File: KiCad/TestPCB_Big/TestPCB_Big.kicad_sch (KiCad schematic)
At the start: 82 parts, among them J2 USB4135-GF-A, Q1 SFH_3711, Q2 2N7002, Q3 2N7002, U1 ESP32-S3-WROOM-1, U1 MCP73831-2-OT, U2 TC1185-xCT, U4 LSM6DSM

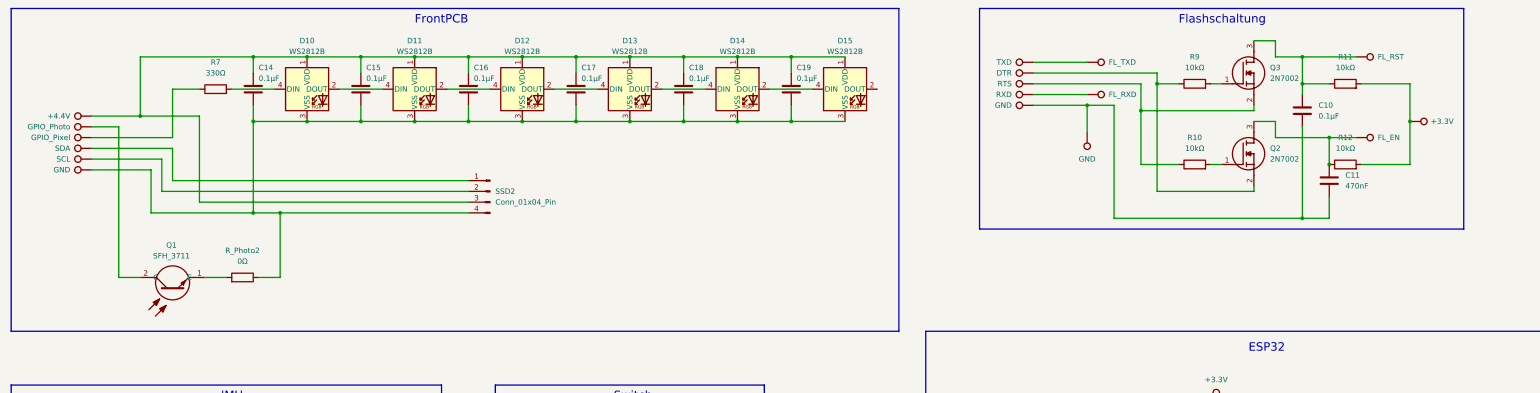
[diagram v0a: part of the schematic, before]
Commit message: CHG: pcb-layouts adopted
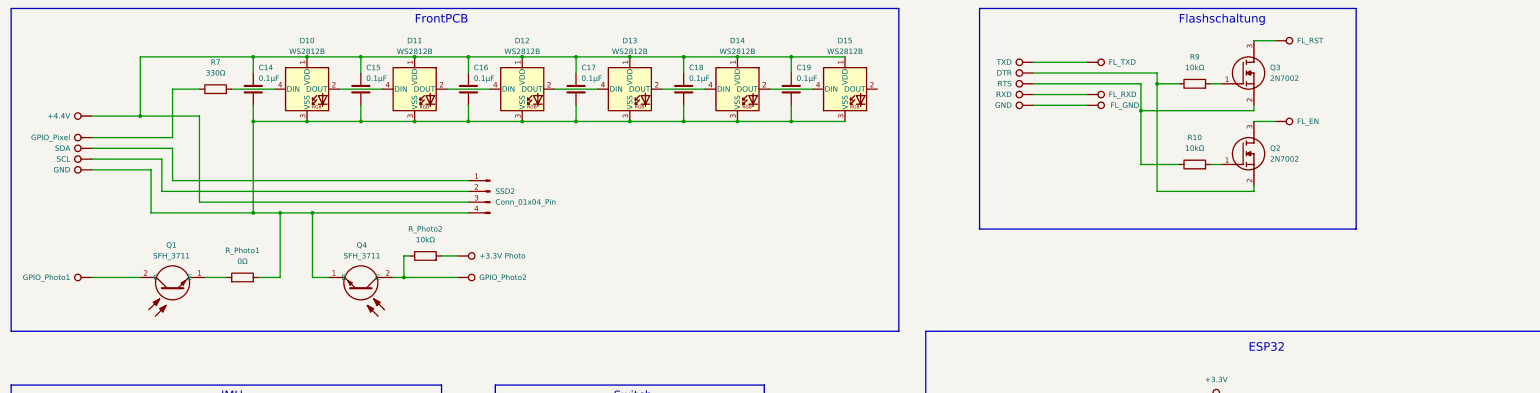
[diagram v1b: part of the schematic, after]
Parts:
- removed C10: 0.1µF, Capacitor_SMD:C_0805_2012Metric, symbol Device:C
- removed C11: 470nF, Capacitor_SMD:C_0805_2012Metric, symbol Device:C
- removed R11, R12: 10kΩ, Resistor_SMD:R_0805_2012Metric, symbol Device:R
- added Q4: SFH_3711, SFH3711, symbol SFH_3711:SFH_3711
- added R_Photo2: 10kΩ, Resistor_SMD:R_0805_2012Metric, symbol Device:R
- added TP39: +3.3V Photo, TestPoint:TestPoint_Pad_2.0x2.0mm, symbol Connector:TestPoint
- TP13: value GND -> FL_GND
- TP31: value GPIO_Photo -> GPIO_Photo1
- TP7: value +3.3V -> GPIO_Photo2
- renumbered R_Photo2 to R_Photo1
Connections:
- net at C14.2, C15.2, C16.2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: now also Q4.1 (E)
- net at TP7.1: now also Q4.2 (C), R_Photo2.1
- new net: R_Photo2.2, TP39.1
